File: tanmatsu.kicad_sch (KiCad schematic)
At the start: 49 parts, among them J1 USB host, J10 External Add-On (SAO / PMOD), J2 Micro_SD_Card, J3 USB device, J4 Headphone, J5 Speaker, J6 CAMERA, J7 SAO, J8 Expansion I3C, J9 Internal Add-On, SW1 Boot, U1 USBLC6-2P6, U2 USBLC6-2P6, U3 CH334R, U4 USBLC6-2P6, U5 ESD, U6 ESD, Y1 12MHz

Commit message: Replace D1 with Elecsuper-CDSOD323T03SC for RoHS compliance
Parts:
- D1: LCSC C5137774 -> C22363742
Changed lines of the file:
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@@
 			)
 		)
-		(property "Datasheet" "https://www.lcsc.com/product-detail/ESD-and-Surge-Protection-TVS-ESD_GOODWORK-ES3-3D1HA03_C5137774.html"
+		(property "Datasheet" "https://jlcpcb.com/partdetail/Elecsuper-CDSOD323T03SC/C22363742"
 			(at 128.27 153.67 0)
 			(effects
@@
 			)
 		)
-		(property "LCSC" "C5137774"
+		(property "LCSC" "C22363742"
 			(at 128.27 153.67 0)
 			(effects

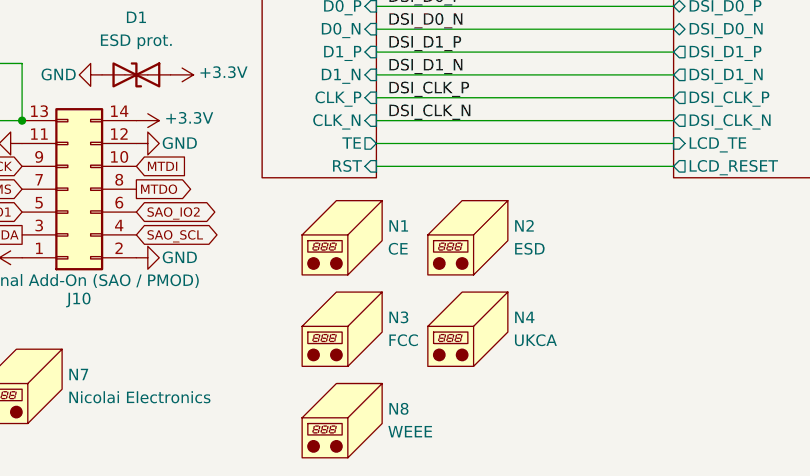
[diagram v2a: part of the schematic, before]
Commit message: Remove CE/FCC/UKCA markings for prototype, switch 22uF capacitor to C602037
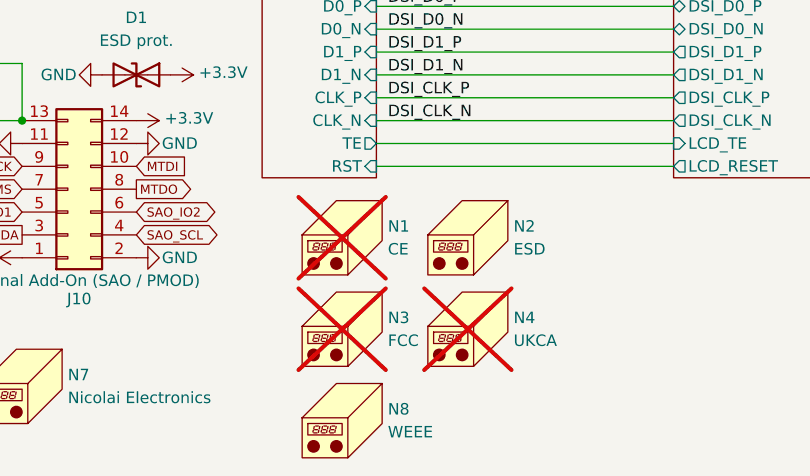
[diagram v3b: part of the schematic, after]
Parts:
- N1, N3, N4: now not fitted
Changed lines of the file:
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@@
 		(exclude_from_sim no)
 		(in_bom no)
-		(on_board yes)
-		(dnp no)
+		(on_board no)
+		(dnp yes)
 		(fields_autoplaced yes)
 		(property "Reference" "N4"
@@
 		(exclude_from_sim no)
 		(in_bom no)
-		(on_board yes)
-		(dnp no)
+		(on_board no)
+		(dnp yes)
 		(fields_autoplaced yes)
 		(property "Reference" "N1"
@@
 		(exclude_from_sim no)
 		(in_bom no)
-		(on_board yes)
-		(dnp no)
+		(on_board no)
+		(dnp yes)
 		(fields_autoplaced yes)
 		(property "Reference" "N3"

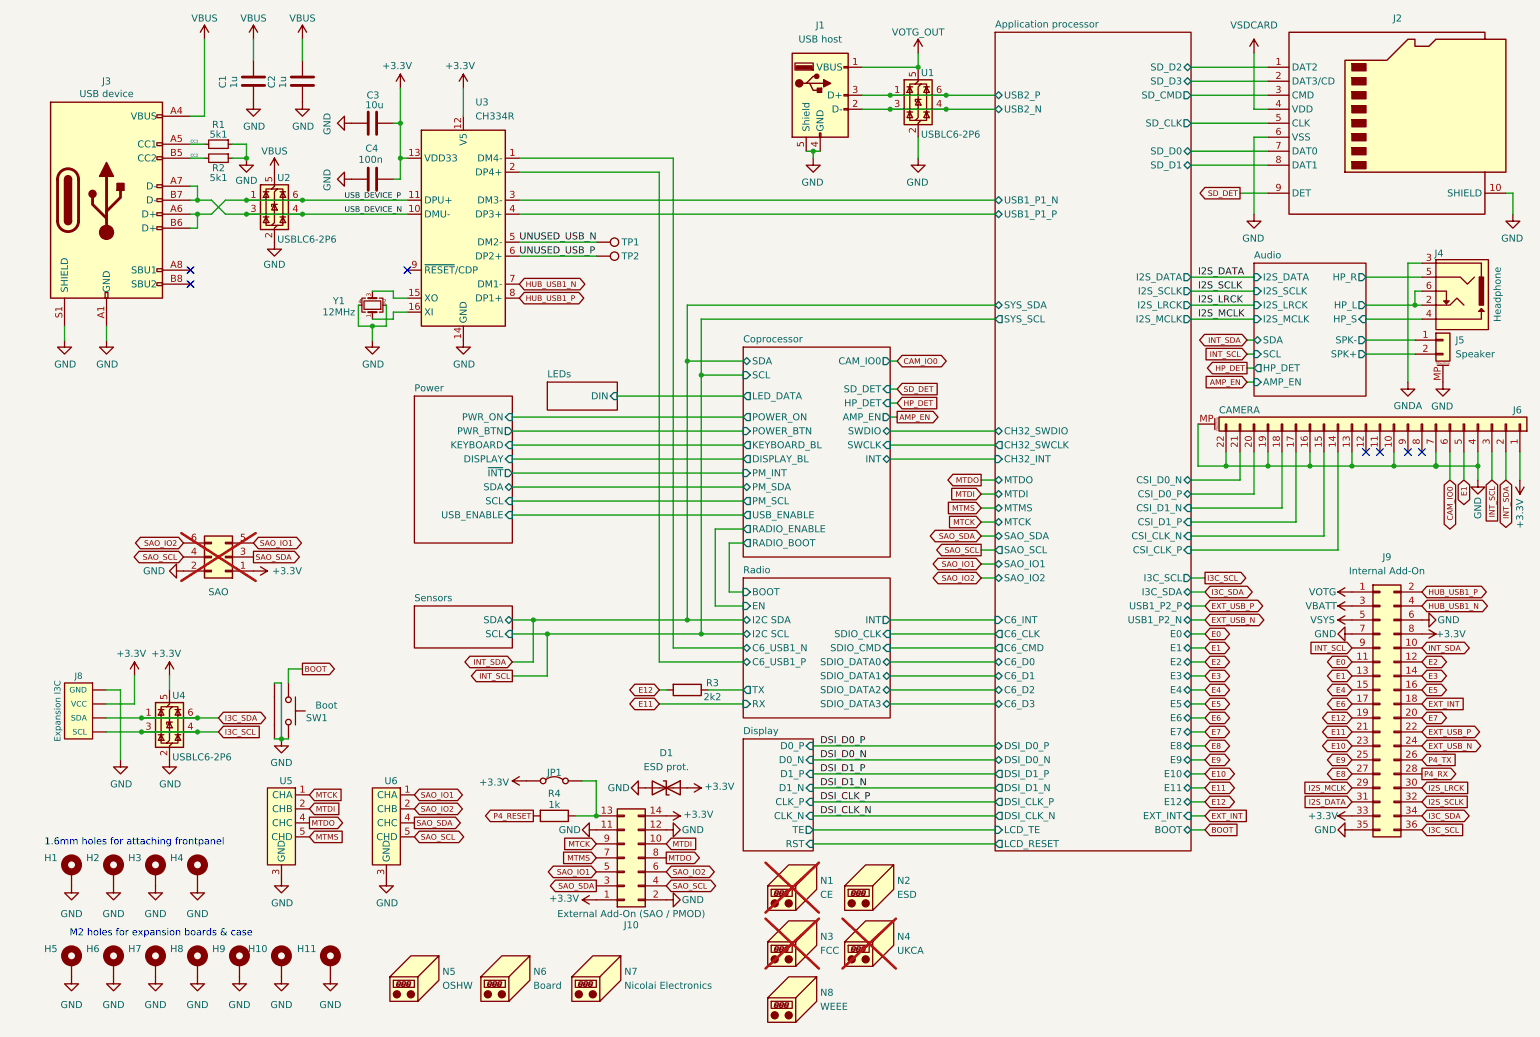
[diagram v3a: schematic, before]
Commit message: Move LoRa module, add capacitor, finalize design for production
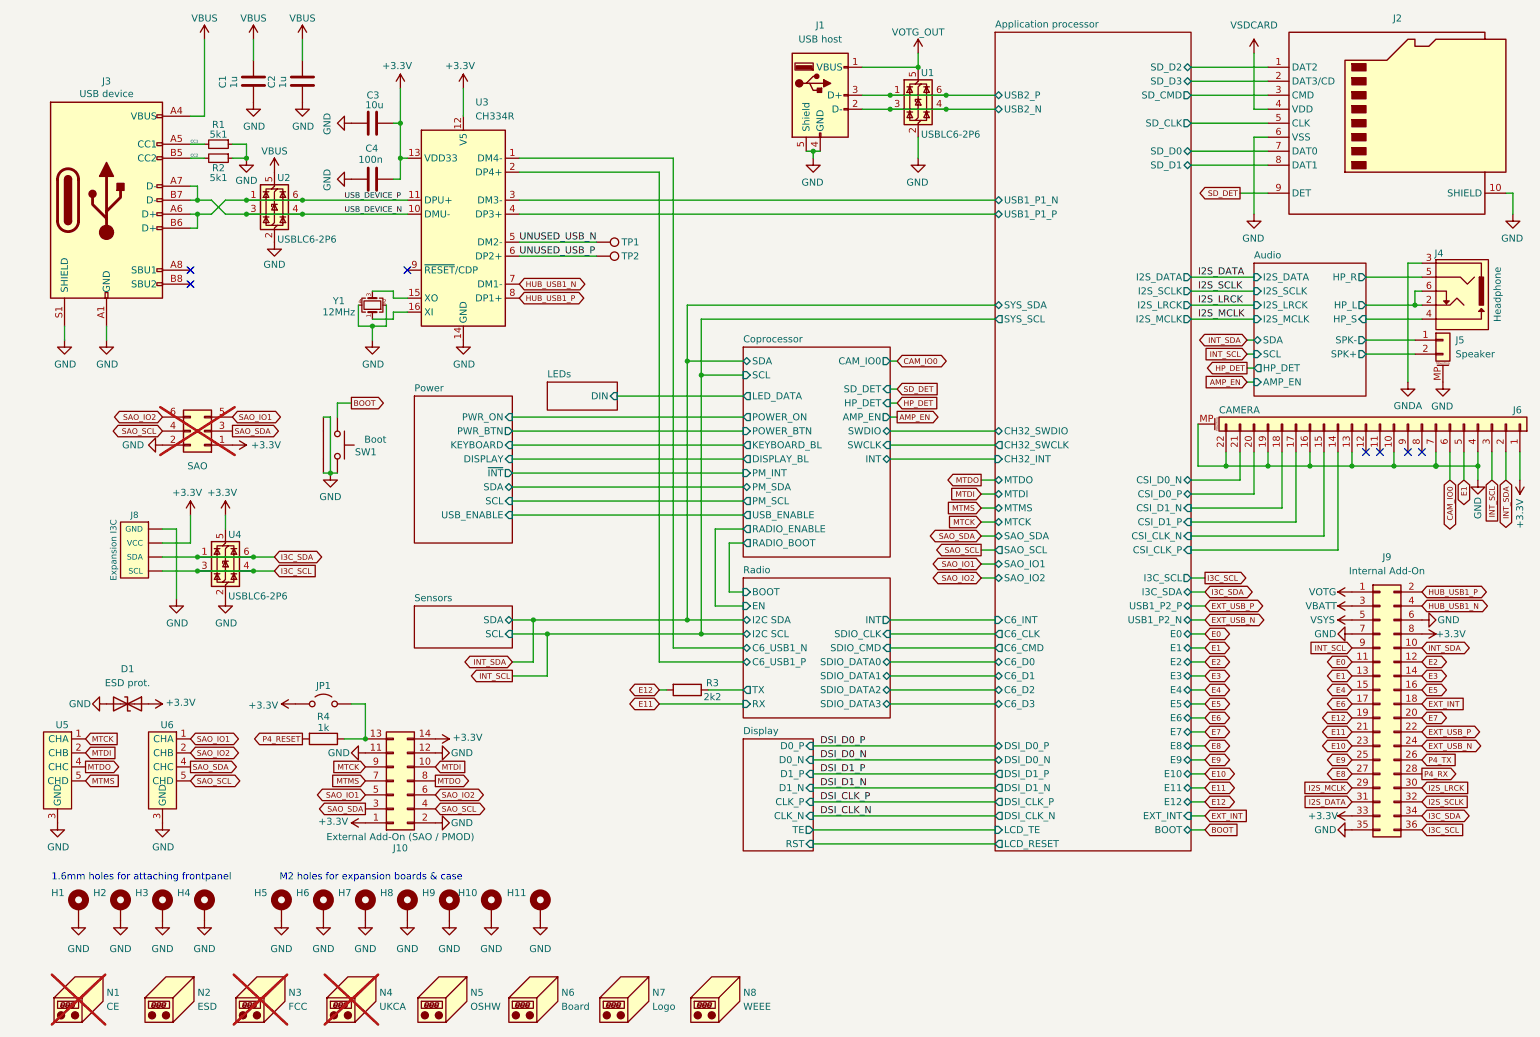
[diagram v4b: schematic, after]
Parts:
- JP1: symbol Jumper:Jumper_2_Bridged -> Jumper:Jumper_2_Open
- N7: value Nicolai Electronics -> Logo
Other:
- moved on the sheet: D1, H1, H10, H11, H2, H3, H4, H5, H6, H7, H8, H9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
